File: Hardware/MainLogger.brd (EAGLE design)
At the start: 98.9 x 72.1 mm, 247 parts, among them J3 GEMS_POWER_PLUGINPUT_RT, J4 U.FL, J5 SIM_CDNANO_SF72, P1:C1 0.1uF, P1:C2 2.2uF, P1:C3 1uF, P1:C4 100uF, P1:C5 0.1uF, P1:J1 CONN_TALON_LOGGER, P1:R1 100k, P1:U1 SN74AUP1G08DCK, P1:U2 FXMAR2102UMLP, P1:U3 FSA2258, P1:U4 AP2411, P2:C1 0.1uF, P2:C2 2.2uF, P2:C3 1uF, P2:C4 100uF, P2:C5 0.1uF, P2:J1 CONN_TALON_LOGGER, P2:R1 100k, P2:U1 SN74AUP1G08DCK, P2:U2 FXMAR2102UMLP, P2:U3 FSA2258, P2:U4 AP2411, P3:C1 0.1uF, P3:C2 2.2uF, P3:C3 1uF, P3:C4 100uF, P3:C5 0.1uF, P3:J1 CONN_TALON_LOGGER, P3:R1 100k, P3:U1 SN74AUP1G08DCK, P3:U2 FXMAR2102UMLP, P3:U3 FSA2258, P3:U4 AP2411, P4:C1 0.1uF, P4:C2 2.2uF, P4:C3 1uF, P4:C4 100uF, P4:C5 0.1uF, P4:J1 CONN_TALON_LOGGER, P4:R1 100k, P4:U1 SN74AUP1G08DCK, P4:U2 FXMAR2102UMLP, P4:U3 FSA2258, P4:U4 AP2411, Q1 DMG3404, Q2 MOSFET_PCH-DMP3036SFG, Q3 MOSFET_PCH-DMP3036SFG, Q4 DMG3404, Q5 NX2301P, Q6 NX2301P, U1 FXMAR2102UMLP, U10 SN74AUP3G34DCU, U11 SIP32431TDFN, U12 LTC4412S6, U13 TCR2LE31ESV, U14 LP59073.3VYKE, U15 MIC22602, U16 BQ25616, U17 TPS61282D, U18 MCP23018QFN, U19 MCP23018QFN, U2 VEML3328, U20 MAX-M8W, U21 MCP79412SOIC, U22 HALL_EFFECT_SI7201, U23 PCA9634QFN, U24 SN74LVC1G17DCK, U25 TPL5010DDC, U26 TPL5010DDC, U27 MB85RC, U28 FXMAR2102UMLP, U3 MMC5633, U4 MXC6655, U5 PAC1934QFN, U6 PAC1934QFN, U7 SHT40, U8 SN74AUP1G08DCK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

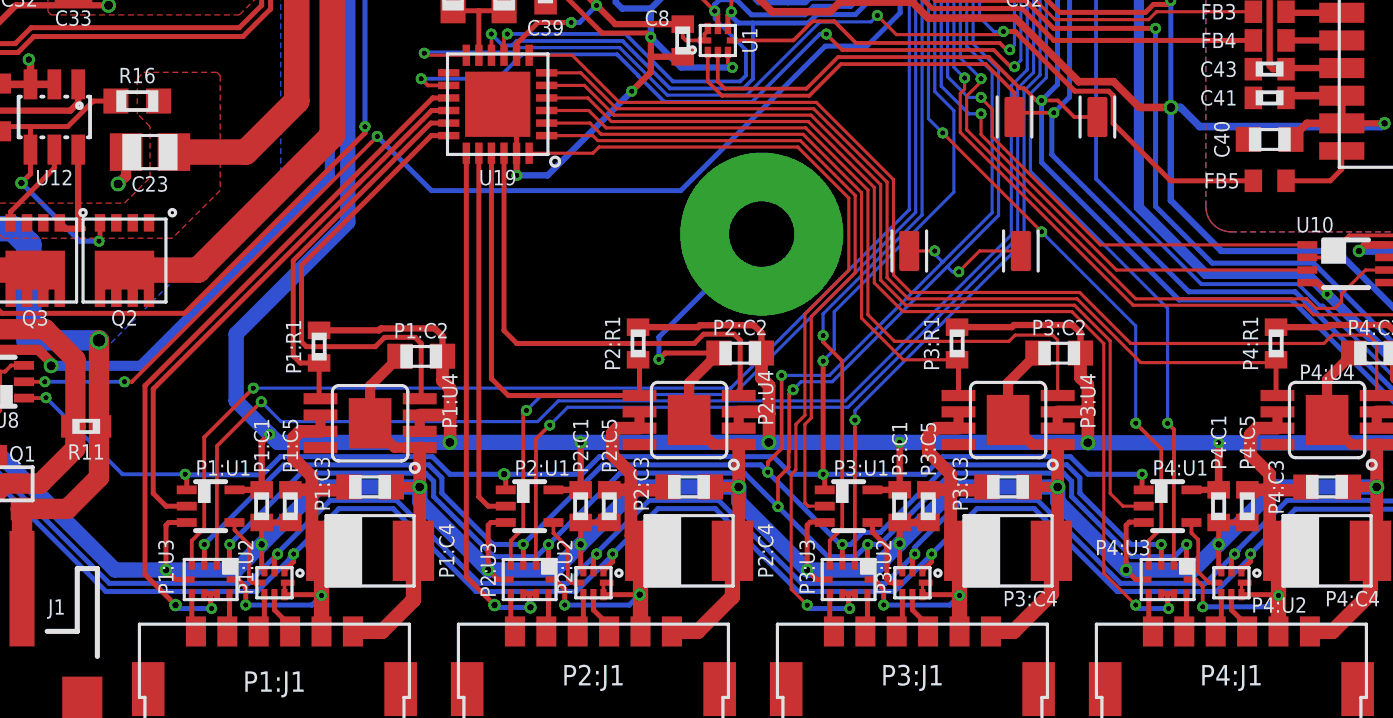
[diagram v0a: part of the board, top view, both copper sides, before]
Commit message: Added series resistors for GPIO output
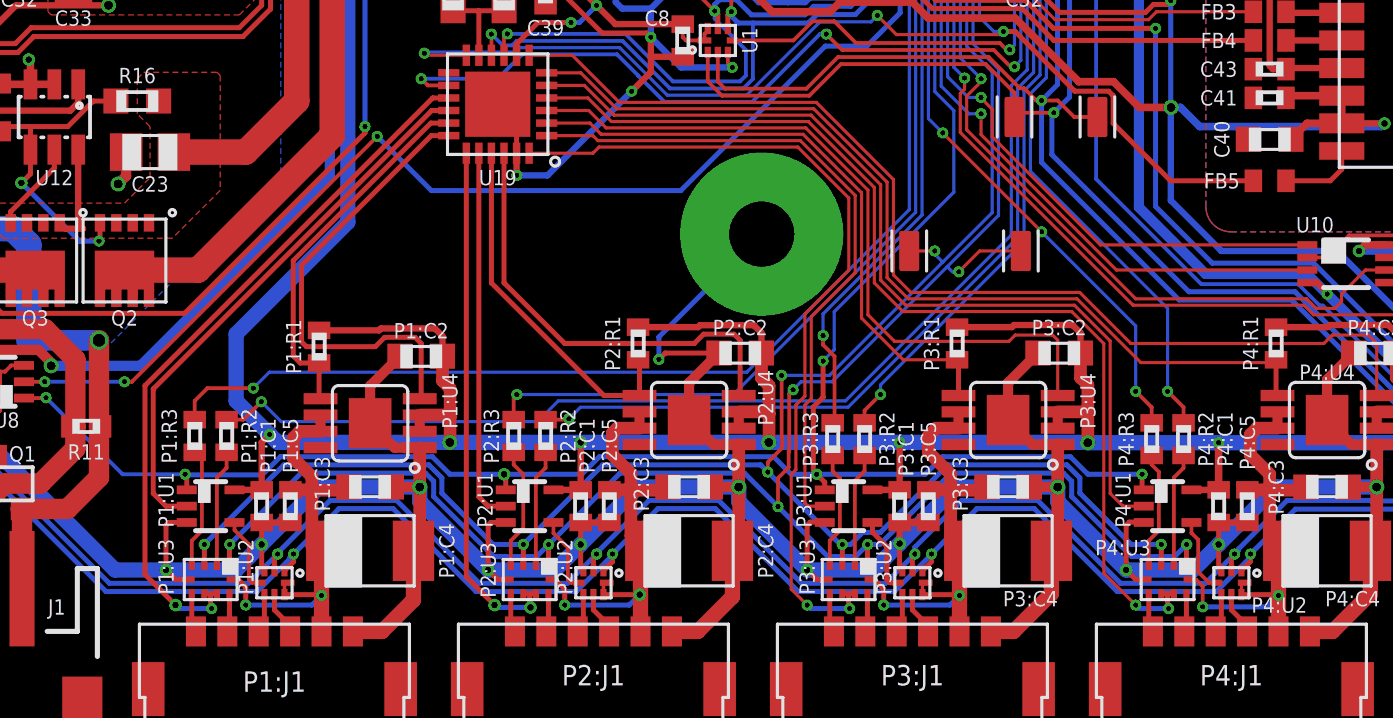
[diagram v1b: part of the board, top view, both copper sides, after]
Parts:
- added P1:R2, P1:R3, P2:R2, P2:R3, P3:R2, P3:R3, P4:R2, P4:R3: 1k, bschulz_passives:R0402
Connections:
- new net P1:N$1: P1:R3.1, P1:U3.4
- new net P1:N$2: P1:R2.1, P1:U3.2
- new net P2:N$1: P2:R3.1, P2:U3.4
- new net P2:N$2: P2:R2.1, P2:U3.2
- new net P3:N$1: P3:R3.1, P3:U3.4
- new net P3:N$2: P3:R2.1, P3:U3.2
- new net P4:N$1: P4:R3.1, P4:U3.4
- new net P4:N$2: P4:R2.1, P4:U3.2
- net TALON1_GPIOA: now also P1:R2.2; no longer P1:U3.2
- net TALON1_GPIOB: now also P1:R3.2; no longer P1:U3.4
- net TALON2_GPIOA: now also P2:R2.2; no longer P2:U3.2
- net TALON2_GPIOB: now also P2:R3.2; no longer P2:U3.4
- net TALON3_GPIOA: now also P3:R2.2; no longer P3:U3.2
- net TALON3_GPIOB: now also P3:R3.2; no longer P3:U3.4
- net TALON4_GPIOA: now also P4:R2.2; no longer P4:U3.2
- net TALON4_GPIOB: now also P4:R3.2; no longer P4:U3.4
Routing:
- net TALON4_GPIOB: track 64.8 -> 58.7 mm
- net TALON3_GPIOB: track 63.0 -> 57.0 mm
- net TALON3_GPIOA: track 66.3 -> 60.4 mm
- net TALON2_GPIOA: track 78.1 -> 72.3 mm
- net TALON1_GPIOA: track 91.0 -> 85.5 mm
- net TALON4_GPIOA: track 67.8 -> 62.3 mm
- net TALON2_GPIOB: track 72.1 -> 66.8 mm
- net P2:N$1: track 0.00 -> 4.87 mm
- net P1:N$1: track 0.00 -> 4.79 mm
- net TALON1_GPIOB: track 84.0 -> 79.2 mm
- net P2:N$2: track 0.00 -> 4.66 mm
- net P1:N$2: track 0.00 -> 4.66 mm
- net P3:N$1: track 0.00 -> 4.66 mm
- net P4:N$1: track 0.00 -> 4.66 mm
- net P4:N$2: track 0.00 -> 4.54 mm
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
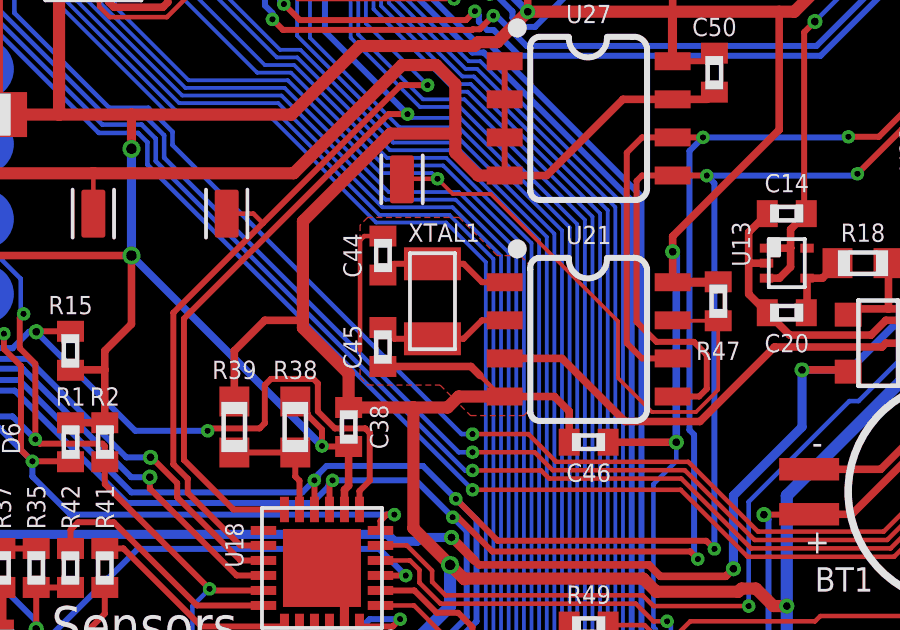
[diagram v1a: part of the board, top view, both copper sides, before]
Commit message: Switched RTC crystal to TCXO
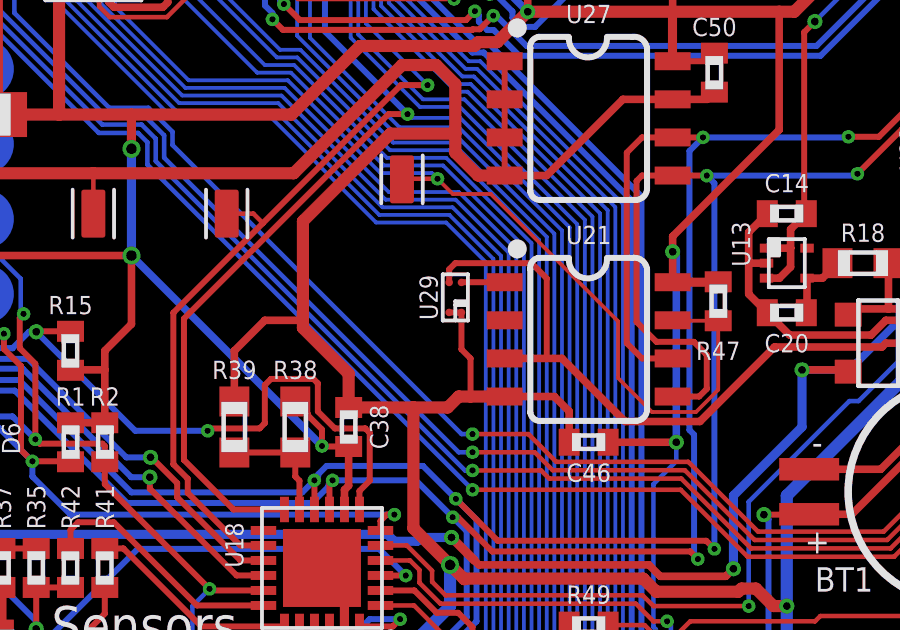
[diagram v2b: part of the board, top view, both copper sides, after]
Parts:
- removed C44, C45: 9pF, bschulz_passives:C0402
- removed XTAL1: CRYSTAL32.768KHZ_9PF3.2X1.5, bschulz:CRYSTAL_3.2X1.5_2-SMD
- added U29: SIT1552, bschulz:LD-4
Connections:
- removed net N$7: C45.1, U21.2, XTAL1.P$2
- net BCKP_RTC: now also U29.3
- net GND: now also U29.1, U29.4; no longer C44.2, C45.2
- net N$4: now also U29.2; no longer C44.1, XTAL1.P$1
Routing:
- net BCKP_RTC: track 15.5 -> 22.2 mm
- net GND: track 918.3 -> 912.6 mm
- net N$7: track 4.47 -> 0.00 mm
- net N$4: track 4.47 -> 1.44 mm
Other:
- board text added: "Project Kestrel v1.2A Bobby Schulz"
- board text removed: "Project Kestrel v1.2 Bobby Schulz"
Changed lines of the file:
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@@
 IN</text>
 <text x="62.992" y="34.544" size="1.27" layer="51" font="vector" ratio="15" align="center-left">Project Kestrel
-v1.2
+v1.2A
 Bobby
 Schulz</text>
@@
 <attribute name="VALUE" x="58.42" y="43.18" size="0.6096" layer="27" font="vector" ratio="15" align="bottom-center"/>
 </element>
-<element name="XTAL1" library="bschulz" package="CRYSTAL_3.2X1.5_2-SMD" value="CRYSTAL32.768KHZ_9PF3.2X1.5" x="53.213" y="48.26" smashed="yes" rot="R270">
-<attribute name="DIGIKEY" value="535-11937-1-ND" x="73.533" y="53.34" size="1.778" layer="27" rot="R270" display="off"/>
-<attribute name="MF" value="ABS07-120-32.768KHZ-T" x="73.533" y="53.34" size="1.778" layer="27" rot="R270" display="off"/>
-<attribute name="MPN" value="Abracon" x="73.533" y="53.34" size="1.778" layer="27" rot="R270" display="off"/>
-<attribute name="NAME" x="53.594" y="50.546" size="0.6096" layer="25" font="vector" ratio="15" align="center"/>
-</element>
-<element name="C44" library="bschulz_passives" package="C0402" value="9pF" x="51.562" y="49.784" smashed="yes" rot="R90">
-<attribute name="DIGIKEY" value="311-3726-1-ND" x="36.322" y="40.894" size="1.778" layer="27" rot="R90" display="off"/>
-<attribute name="MF" value="Yageo" x="36.322" y="40.894" size="1.778" layer="27" rot="R90" display="off"/>
-<attribute name="MPN" value="CC0402DRNPO9BN9R0" x="36.322" y="40.894" size="1.778" layer="27" rot="R90" display="off"/>
-<attribute name="NAME" x="50.546" y="49.784" size="0.6096" layer="25" font="vector" ratio="15" rot="R90" align="center"/>
-<attribute name="VALUE" x="52.578" y="49.784" size="0.6096" layer="27" font="vector" ratio="15" rot="R90" align="center"/>
-</element>
-<element name="C45" library="bschulz_passives" package="C0402" value="9pF" x="51.562" y="46.736" smashed="yes" rot="R270">
-<attribute name="DIGIKEY" value="311-3726-1-ND" x="62.992" y="59.436" size="1.778" layer="27" rot="R270" display="off"/>
-<attribute name="MF" value="Yageo" x="62.992" y="59.436" size="1.778" layer="27" rot="R270" display="off"/>
-<attribute name="MPN" value="CC0402DRNPO9BN9R0" x="62.992" y="59.436" size="1.778" layer="27" rot="R270" display="off"/>
-<attribute name="NAME" x="50.546" y="46.736" size="0.6096" layer="25" font="vector" ratio="15" rot="R270" align="center"/>
-<attribute name="VALUE" x="50.165" y="46.355" size="0.6096" layer="27" font="vector" ratio="15" rot="R270" align="center"/>
-</element>
 <element name="C46" library="bschulz_passives" package="C0402" value="0.1uF" x="58.42" y="43.561" smashed="yes" rot="R180">
 <attribute name="DIGIKEY" value="490-4759-1-ND" x="62.23" y="51.181" size="1.778" layer="27" rot="R180" display="off"/>
@@
 <attribute name="VALUE_PART" value="1k" x="64.135" y="13.335" size="1.778" layer="27" rot="R90" display="off"/>
 </element>
+<element name="U29" library="bschulz" package="LD-4" value="SIT1552" x="53.975" y="48.387" smashed="yes" rot="R90">
+<attribute name="DIGIKEY" value="1473-1242-1-ND" x="53.975" y="48.387" size="1.778" layer="27" rot="R90" display="off"/>
+<attribute name="DISP" value="SiT1552" x="53.975" y="48.387" size="1.778" layer="27" rot="R90" display="off"/>
+<attribute name="MF" value="SiTime" x="53.975" y="48.387" size="1.778" layer="27" rot="R90" display="off"/>
+<attribute name="MPN" value="SIT1552AI-JF-DCC-32.768D" x="53.975" y="48.387" size="1.778" layer="27" rot="R90" display="off"/>
+<attribute name="NAME" x="53.086" y="48.387" size="0.6096" layer="25" font="vector" ratio="15" rot="R90" align="center"/>
+</element>
 </elements>
 <signals>
@@
 <contactref element="U13" pad="2"/>
 <contactref element="BT1" pad="-"/>
-<contactref element="C44" pad="2"/>
-<contactref element="C45" pad="2"/>
 <contactref element="U21" pad="4"/>
 <contactref element="C46" pad="2"/>
@@
 <contactref element="SD1" pad="BODY@3"/>
 <contactref element="SD1" pad="SW1"/>
-<polygon width="0.2" layer="1" thermals="no">
-<vertex x="56.134" y="49.784"/>
-<vertex x="55.372" y="49.784"/>
-<vertex x="54.102" y="51.054"/>
-<vertex x="51.054" y="51.054"/>
-<vertex x="50.8" y="50.8"/>
-<vertex x="50.8" y="45.72"/>
-<vertex x="51.054" y="45.466"/>
-<vertex x="53.467" y="45.466"/>
-<vertex x="54.483" y="44.45"/>
-<vertex x="56.261" y="44.45"/>
-<vertex x="56.515" y="44.704"/>
-<vertex x="56.515" y="49.403"/>
-</polygon>
 <contactref element="U14" pad="B2"/>
 <contactref element="C22" pad="2"/>
@@
 <wire x1="75.946" y1="53.34" x2="74.84" y2="53.34" width="0.254" layer="1"/>
 <wire x1="74.84" y1="53.34" x2="72.39" y2="53.34" width="0.254" layer="1"/>
-<wire x1="51.45" y1="45.974" x2="51.562" y2="46.086" width="0.4064" layer="1"/>
 <wire x1="48.895" y1="50.927" x2="48.895" y2="47.625" width="0.4064" layer="1"/>
 <wire x1="48.895" y1="47.625" x2="48.895" y2="47.371" width="0.4064" layer="1"/>
@@
 <wire x1="44.5174" y1="17.4064" x2="48.611" y2="21.5" width="0.2" layer="16"/>
 <wire x1="53.721" y1="44.719" x2="54.087" y2="45.085" width="0.4064" layer="1"/>
-<wire x1="54.087" y1="45.085" x2="55.62" y2="45.085" width="0.4064" layer="1"/>
-<wire x1="51.562" y1="50.434" x2="50.942" y2="50.434" width="0.1524" layer="1"/>
-<wire x1="50.942" y1="50.434" x2="50.8" y2="50.292" width="0.1524" layer="1"/>
-<wire x1="50.8" y1="50.292" x2="50.8" y2="46.624" width="0.1524" layer="1"/>
+<wire x1="54.087" y1="45.085" x2="54.483" y2="45.085" width="0.4064" layer="1"/>
+<wire x1="54.483" y1="45.085" x2="55.62" y2="45.085" width="0.4064" layer="1"/>
 <wire x1="55.499" y1="45.085" x2="55.62" y2="45.085" width="0.1524" layer="1"/>
-<wire x1="54.8005" y1="45.7835" x2="55.499" y2="45.085" width="0.1524" layer="1"/>
 <wire x1="49.53" y1="39.37" x2="50.28" y2="38.62" width="0.3048" layer="1"/>
 <wire x1="50.28" y1="38.62" x2="50.28" y2="37.42" width="0.3048" layer="1"/>
@@
 <wire x1="20.32" y1="42.545" x2="20.574" y2="42.291" width="0.2" layer="1"/>
 <wire x1="20.32" y1="42.545" x2="20.32" y2="42.941" width="0.2" layer="1"/>
-<wire x1="51.562" y1="46.086" x2="54.498" y2="46.086" width="0.254" layer="1"/>
-<wire x1="54.498" y1="46.086" x2="54.8005" y2="45.7835" width="0.254" layer="1"/>
 <wire x1="13.6786" y1="67.2956" x2="13.6786" y2="63.0294" width="0.508" layer="1"/>
 <wire x1="13.6786" y1="63.0294" x2="13.843" y2="62.865" width="0.508" layer="1"/>
@@
 <wire x1="59.182" y1="35.2572375" x2="59.8601625" y2="35.2572375" width="0.2" layer="1"/>
 <wire x1="60.286725" y1="35.6838" x2="61.137875" y2="35.6838" width="0.2" layer="1"/>
+<contactref element="U29" pad="1"/>
+<contactref element="U29" pad="4"/>
+<wire x1="53.77" y1="47.887" x2="54.18" y2="47.887" width="0.2" layer="1"/>
+<wire x1="54.18" y1="47.887" x2="54.18" y2="46.658" width="0.2" layer="1"/>
+<wire x1="54.483" y1="46.355" x2="54.483" y2="45.085" width="0.2" layer="1"/>
+<wire x1="54.18" y1="46.658" x2="54.483" y2="46.355" width="0.2" layer="1"/>
 </signal>
 <signal name="D+">
@@
 <wire x1="69.172" y1="46.863" x2="68.326" y2="46.863" width="0.254" layer="1"/>
 <wire x1="68.326" y1="46.863" x2="68.199" y2="46.736" width="0.254" layer="1"/>
-<wire x1="57.531" y1="46.355" x2="55.62" y2="46.355" width="0.254" layer="1"/>
+<wire x1="57.531" y1="46.355" x2="57.023" y2="46.355" width="0.254" layer="1"/>
+<wire x1="57.023" y1="46.355" x2="55.62" y2="46.355" width="0.254" layer="1"/>
 <wire x1="68.199" y1="46.736" x2="64.61385" y2="46.736" width="0.254" layer="1"/>
 <wire x1="64.61385" y1="46.736" x2="62.12945" y2="44.2516" width="0.254" layer="1"/>
 <wire x1="62.12945" y1="44.2516" x2="59.6344" y2="44.2516" width="0.254" layer="1"/>
 <wire x1="59.6344" y1="44.2516" x2="57.531" y2="46.355" width="0.254" layer="1"/>
+<contactref element="U29" pad="3"/>
+<wire x1="53.77" y1="48.887" x2="53.77" y2="49.325" width="0.2" layer="1"/>
+<wire x1="53.77" y1="49.325" x2="53.975" y2="49.53" width="0.2" layer="1"/>
+<wire x1="53.975" y1="49.53" x2="56.515" y2="49.53" width="0.2" layer="1"/>
+<wire x1="56.515" y1="49.53" x2="57.023" y2="49.022" width="0.2" layer="1"/>
+<wire x1="57.023" y1="49.022" x2="57.023" y2="46.355" width="0.2" layer="1"/>
 </signal>
 <signal name="3V3_AUX" class="1">
@@
 <wire x1="60.4624" y1="30.3276" x2="63.891725" y2="30.3276" width="0.2" layer="1"/>
 </signal>
-<signal name="N$4">
-<contactref element="U21" pad="1"/>
-<contactref element="XTAL1" pad="P$1"/>
-<contactref element="C44" pad="1"/>
-<wire x1="51.562" y1="49.134" x2="51.938" y2="49.51" width="0.2" layer="1"/>
-<wire x1="51.938" y1="49.51" x2="53.213" y2="49.51" width="0.2" layer="1"/>
-<wire x1="53.213" y1="49.51" x2="54.249" y2="49.51" width="0.2" layer="1"/>
-<wire x1="54.864" y1="48.895" x2="55.62" y2="48.895" width="0.2" layer="1"/>
-<wire x1="54.249" y1="49.51" x2="54.864" y2="48.895" width="0.2" layer="1"/>
-</signal>
-<signal name="N$7">
-<contactref element="U21" pad="2"/>
-<contactref element="XTAL1" pad="P$2"/>
-<contactref element="C45" pad="1"/>
-<wire x1="51.562" y1="47.386" x2="51.938" y2="47.01" width="0.2" layer="1"/>
-<wire x1="51.938" y1="47.01" x2="53.213" y2="47.01" width="0.2" layer="1"/>
-<wire x1="53.213" y1="47.01" x2="54.249" y2="47.01" width="0.2" layer="1"/>
-<wire x1="54.864" y1="47.625" x2="55.62" y2="47.625" width="0.2" layer="1"/>
-<wire x1="54.249" y1="47.01" x2="54.864" y2="47.625" width="0.2" layer="1"/>
-</signal>
 <signal name="RTC_INT">
 <contactref element="U21" pad="7"/>
@@
 <wire x1="65.405" y1="12.192" x2="65.02" y2="11.807" width="0.1524" layer="1"/>
 </signal>
+<signal name="N$4">
+<contactref element="U29" pad="2"/>
+<contactref element="U21" pad="1"/>
+<wire x1="54.18" y1="48.887" x2="54.188" y2="48.895" width="0.2" layer="1"/>
+<wire x1="54.188" y1="48.895" x2="55.62" y2="48.895" width="0.2" layer="1"/>
+</signal>
 </signals>

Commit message: Fixed passive value, added BoM
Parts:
- R49: value (none) -> 100k
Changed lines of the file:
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@@
 <attribute name="VALUE" x="69.215" y="69.088" size="0.6096" layer="27" font="vector" ratio="15" rot="R180" align="center"/>
 </element>
-<element name="R49" library="bschulz_passives" package="R0402" value="" x="58.42" y="37.465" smashed="yes">
+<element name="R49" library="bschulz_passives" package="R0402" value="100k" x="58.42" y="37.465" smashed="yes">
 <attribute name="DIGIKEY" value="311-100KLRCT-ND" x="58.42" y="37.465" size="1.778" layer="27" display="off"/>
 <attribute name="MF" value="Yageo" x="58.42" y="37.465" size="1.778" layer="27" display="off"/>

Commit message: v1.3 Updates
Reconfigured backup battery charger
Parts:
- added D19: (no value), bschulz:SOD323-R
- R18: value 1k -> 750R
- moved R18 4.54 mm to (71.6, 47.5), turned to 270 degrees
- moved C14 1.28 mm to (63.8, 51.1)
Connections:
- new net N$7: BT1.+, R18.2
- net BCKP_GPS: now also D19.C, R18.1; no longer BT1.+, R18.2
- net N$3: now also D19.A; no longer R18.1
- net SYS: no longer C14.1, U13.1, U13.3
- net VBULK: now also C14.1, U13.1, U13.3
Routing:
- net SYS: track 140.1 -> 38.9 mm, vias 2 -> 0
- net VBULK: track 122.4 -> 147.4 mm, vias 15 -> 16
- net N$7: track 0.00 -> 9.43 mm
- net !MODE: track 27.3 -> 25.1 mm
- net BCKP_GPS: track 39.1 -> 37.7 mm
- net BAT_CHG: track 121.5 -> 120.6 mm
- net !RESET: track 118.0 -> 118.7 mm
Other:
- board text added: "Project Kestrel v1.3 Bobby Schulz"
- board text removed: "Project Kestrel v1.2A Bobby Schulz"
